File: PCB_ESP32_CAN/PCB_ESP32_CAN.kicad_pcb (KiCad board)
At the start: 2 copper layers, 52.1 x 57.2 mm, 53 parts, among them J1 USB_C_Receptacle_USB2.0, J2 CAN, J3 CAN, J4 CAN, J5 CAN, Q1 Q_NPN_BCE, Q2 Q_NPN_BCE, U1 ESP32-WROOM-32, U2 CP2102N-A01-GQFN24, U3 SN65HVD232, U4 NCP1117-3.3_SOT223

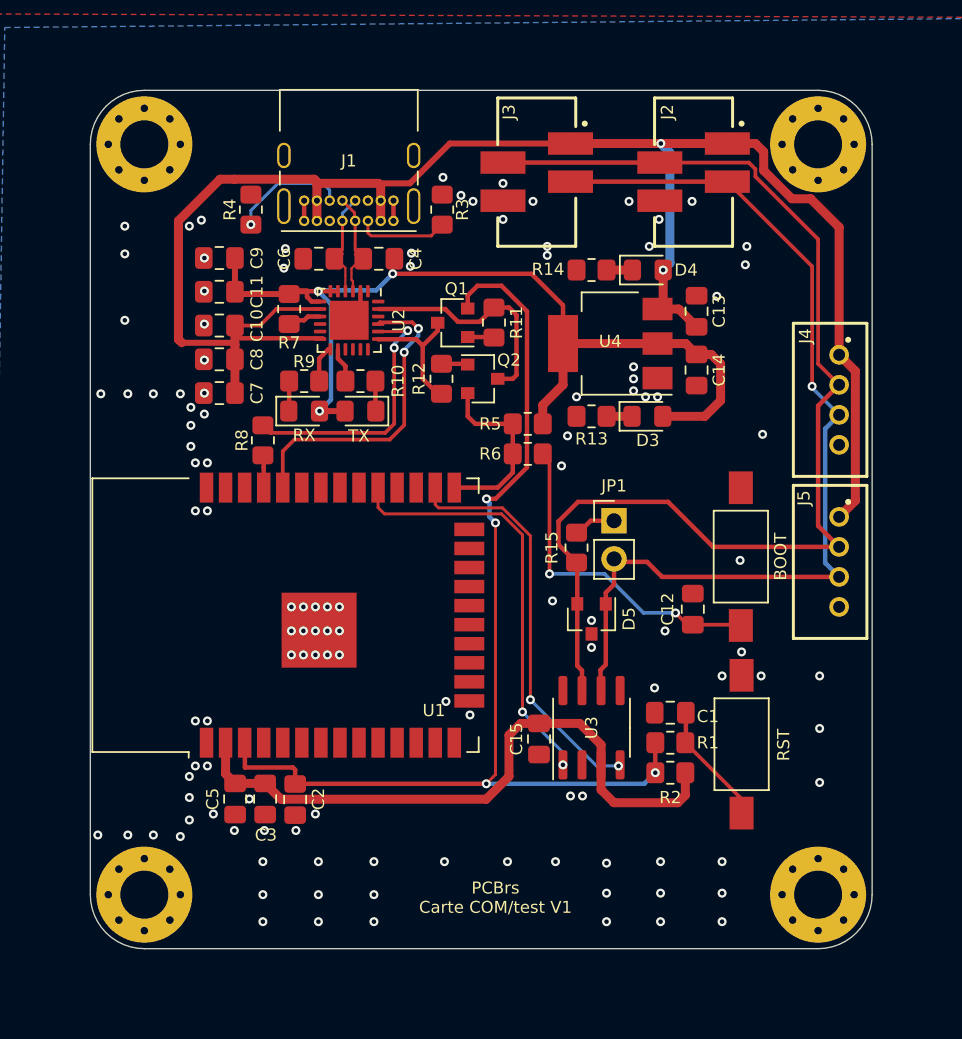
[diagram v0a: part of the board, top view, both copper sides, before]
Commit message: pcb lidar/ax12/batt ready to fab
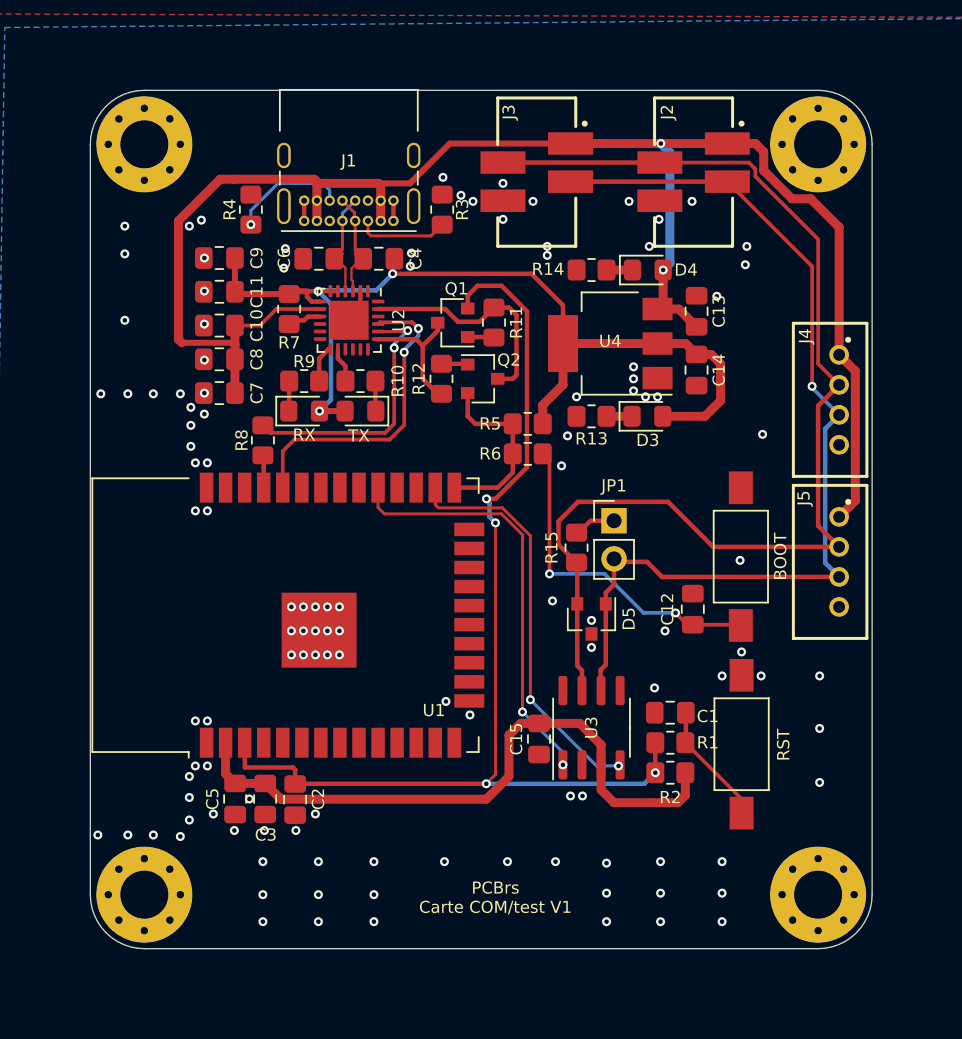
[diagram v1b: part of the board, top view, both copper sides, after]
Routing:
- net Net-(U2-Pad12): track 5.52 -> 0.00 mm
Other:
- net class Default removed

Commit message: V2.0 ESP32 pcb
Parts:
- removed J4, J5: CAN, AREA_lib_Connector:Wuerth_2mm_4pin_62000411622
- removed R1, R6: 560, Resistor_SMD:R_0805_2012Metric_Pad1.20x1.40mm_HandSolder
- removed R5: 10K, Resistor_SMD:R_0805_2012Metric_Pad1.20x1.40mm_HandSolder
- added C16: 10u, Capacitor_SMD:C_0805_2012Metric_Pad1.18x1.45mm_HandSolder, F.Cu at (156.1, 123.2)
- added CANH: CANH, TestPoint:TestPoint_THTPad_D1.0mm_Drill0.5mm, F.Cu at (158.3, 101.6)
- added CANL: CANL, TestPoint:TestPoint_THTPad_D1.0mm_Drill0.5mm, F.Cu at (158.3, 103.5)
- added DTR: DTR, TestPoint:TestPoint_Pad_D1.0mm, F.Cu at (136.4, 86.2)
- added R16: 47k5, Resistor_SMD:R_0805_2012Metric_Pad1.20x1.40mm_HandSolder, F.Cu at (123.7, 90.7)
- added R17: 10k, Resistor_SMD:R_0805_2012Metric_Pad1.20x1.40mm_HandSolder, F.Cu at (123.7, 88.7)
- added RTS: RTS, TestPoint:TestPoint_Pad_D1.0mm, F.Cu at (135.5, 90.2)
- added RX: RX, TestPoint:TestPoint_Pad_D1.0mm, F.Cu at (131.2, 118.9)
- added TX: TX, TestPoint:TestPoint_Pad_D1.0mm, F.Cu at (131.2, 115.7)
- C1, C12, C2: value 1n -> 100n
- R10: value 260 -> 270
- R7: value 10K -> 22k1
- moved C5 93.9 mm to (156.1, 121.2), turned to 0 degrees
- moved C3 91.8 mm to (156.1, 119.2), turned to 0 degrees
- moved C2 89.8 mm to (156.1, 117.2), turned to 180 degrees
- moved J3 80.9 mm to (160.4, 96.4), turned to 180 degrees
- moved U1 75.8 mm to (143.8, 114.5), turned to 180 degrees
- moved R8 68.7 mm to (129.0, 115.7)
- moved J2 68.4 mm to (160.4, 86.0), turned to 180 degrees
- moved R15 65.8 mm to (150.8, 99.2), turned to 0 degrees
- moved 120 65.1 mm to (152.5, 101.7), turned to -90 degrees
- moved C10 63.2 mm to (123.7, 94.7)
- moved C8 63.2 mm to (123.7, 96.8)
- moved C7 63.1 mm to (123.7, 98.8)
- moved C9 62.6 mm to (123.7, 84.7)
- moved C11 62.6 mm to (123.7, 86.7)
- moved R10 61.8 mm to (132.2, 93.5)
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- renumbered JP1 to 120, D3 to 3V3, D4 to 5V, RST to RESET
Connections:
- BOOT pad 1: Net-(C12-Pad1) -> /IO0
- C1 pad 1: Net-(C1-Pad1) -> /EN
- C12 pad 1: Net-(C12-Pad1) -> /IO0
- J1 pad A8: Net-(J1-PadA8) -> unconnected-(J1-PadA8)
- J1 pad B8: Net-(J1-PadB8) -> unconnected-(J1-PadB8)
- R10 pad 1: Net-(D2-Pad1) -> Net-(D2-Pad2)
- R7 pad 1: +3V3 -> +5V
- R7 pad 2: Net-(R7-Pad2) -> Net-(R16-Pad1)
- R9 pad 1: Net-(D1-Pad1) -> Net-(D1-Pad2)
- RESET pad 1: Net-(C1-Pad1) -> GND
- RESET pad 2: GND -> /EN
- RX pad 1: Net-(D1-Pad1) -> GND
- RX pad 2: +3V3 -> Net-(D1-Pad2)
- TX pad 1: Net-(D2-Pad1) -> GND
- TX pad 2: +3V3 -> Net-(D2-Pad2)
- U1 pad 10: Net-(U1-Pad10) -> unconnected-(U1-Pad10)
- U1 pad 11: Net-(U1-Pad11) -> unconnected-(U1-Pad11)
- U1 pad 12: Net-(U1-Pad12) -> unconnected-(U1-Pad12)
- U1 pad 13: Net-(U1-Pad13) -> unconnected-(U1-Pad13)
- U1 pad 14: Net-(U1-Pad14) -> unconnected-(U1-Pad14)
- U1 pad 16: Net-(U1-Pad16) -> unconnected-(U1-Pad16)
- U1 pad 17: Net-(U1-Pad17) -> unconnected-(U1-Pad17)
- U1 pad 18: Net-(U1-Pad18) -> unconnected-(U1-Pad18)
- U1 pad 19: Net-(U1-Pad19) -> unconnected-(U1-Pad19)
- U1 pad 20: Net-(U1-Pad20) -> unconnected-(U1-Pad20)
- U1 pad 21: Net-(U1-Pad21) -> unconnected-(U1-Pad21)
- U1 pad 22: Net-(U1-Pad22) -> unconnected-(U1-Pad22)
- U1 pad 23: Net-(U1-Pad23) -> unconnected-(U1-Pad23)
- U1 pad 24: Net-(U1-Pad24) -> unconnected-(U1-Pad24)
- U1 pad 27: Net-(U1-Pad27) -> unconnected-(U1-Pad27)
- U1 pad 28: Net-(U1-Pad28) -> unconnected-(U1-Pad28)
- U1 pad 30: Net-(U1-Pad30) -> unconnected-(U1-Pad30)
- U1 pad 31: Net-(U1-Pad31) -> unconnected-(U1-Pad31)
- U1 pad 32: Net-(U1-Pad32) -> unconnected-(U1-Pad32)
- U1 pad 33: Net-(U1-Pad33) -> unconnected-(U1-Pad33)
- U1 pad 36: Net-(U1-Pad36) -> unconnected-(U1-Pad36)
- U1 pad 37: Net-(U1-Pad37) -> unconnected-(U1-Pad37)
- U1 pad 4: Net-(U1-Pad4) -> unconnected-(U1-Pad4)
- U1 pad 5: Net-(U1-Pad5) -> unconnected-(U1-Pad5)
- U1 pad 6: Net-(U1-Pad6) -> unconnected-(U1-Pad6)
- U1 pad 7: Net-(U1-Pad7) -> unconnected-(U1-Pad7)
- U1 pad 8: Net-(U1-Pad8) -> unconnected-(U1-Pad8)
- U1 pad 9: Net-(U1-Pad9) -> unconnected-(U1-Pad9)
- U2 pad 1: Net-(U2-Pad1) -> unconnected-(U2-Pad1)
- U2 pad 10: Net-(U2-Pad10) -> unconnected-(U2-Pad10)
- U2 pad 11: Net-(U2-Pad11) -> unconnected-(U2-Pad11)
- U2 pad 12: Net-(U2-Pad12) -> unconnected-(U2-Pad12)
- U2 pad 15: Net-(U2-Pad15) -> unconnected-(U2-Pad15)
- U2 pad 16: Net-(U2-Pad16) -> unconnected-(U2-Pad16)
- U2 pad 17: Net-(U2-Pad17) -> unconnected-(U2-Pad17)
- U2 pad 18: Net-(U2-Pad18) -> unconnected-(U2-Pad18)
- U2 pad 22: Net-(U2-Pad22) -> unconnected-(U2-Pad22)
- U2 pad 24: Net-(U2-Pad24) -> unconnected-(U2-Pad24)
- U2 pad 5: +3V3 -> unconnected-(U2-Pad5)
- U2 pad 8: +5V -> Net-(R16-Pad1)
- U2 pad 9: Net-(R7-Pad2) -> Net-(U2-Pad9)
- U3 pad 5: Net-(U3-Pad5) -> unconnected-(U3-Pad5)
- U3 pad 8: Net-(U3-Pad8) -> unconnected-(U3-Pad8)
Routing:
- net +5V: track 112.2 -> 9.81 mm, vias 2 -> 11
- net +3V3: track 108.1 -> 35.7 mm, vias 3 -> 14
- net /CANH: track 78.0 -> 32.6 mm
- net /CANL: track 65.3 -> 37.5 mm, vias 1 -> 0
- net /IO0: track 12.3 -> 37.5 mm, vias 0 -> 3
- net Net-(C12-Pad1): track 22.4 -> 0.00 mm, vias 2 -> 0
- net /RXCAN: track 27.2 -> 9.71 mm, vias 2 -> 0
- net /TX: track 21.0 -> 36.1 mm
- net Net-(R8-Pad2): track 17.8 -> 29.1 mm
- net /EN: track 71.6 -> 82.2 mm
- net Net-(C1-Pad1): track 8.26 -> 0.00 mm
- net /TXCAN: track 28.1 -> 20.5 mm, vias 2 -> 0
- net Net-(R16-Pad1): track 0.00 -> 6.97 mm
- net Net-(U2-Pad9): track 0.00 -> 6.20 mm, vias 0 -> 2
- net /RX: track 2.31 -> 7.25 mm
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- added copper zone on In1.Cu, net +3V3
- added copper zone on In1.Cu, net +5V
- added copper zone on In2.Cu, net GND
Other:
- copper layers 2 -> 4
- board text added: "."
- board text added: "PCBrs Carte COM V2 IP : 192.168.4.1"
- board text removed: "PCBrs Carte COM/test V1"

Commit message: update
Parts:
- C1, C10, C11, C12, C13, C14, C15, C16, C2, C3, C4, C5, C6, C7, C8, C9: footprint Capacitor_SMD:C_0805_2012Metric_Pad1.18x1.45mm_HandSolder -> Capacitor_SMD:C_0805_2012Metric
- D1: renamed from RX; footprint LED_SMD:LED_0805_2012Metric_Pad1.15x1.40mm_HandSolder -> LED_SMD:LED_0805_2012Metric
- D2: renamed from TX; footprint LED_SMD:LED_0805_2012Metric_Pad1.15x1.40mm_HandSolder -> LED_SMD:LED_0805_2012Metric
- D3: renamed from 3V3; footprint LED_SMD:LED_0805_2012Metric_Pad1.15x1.40mm_HandSolder -> LED_SMD:LED_0805_2012Metric
- D4: renamed from 5V; footprint LED_SMD:LED_0805_2012Metric_Pad1.15x1.40mm_HandSolder -> LED_SMD:LED_0805_2012Metric
- Q1, Q2: value Q_NPN_BCE -> MMBT2222ALT1G
- R10, R11, R12, R13, R14, R15, R16, R17, R2, R3, R4, R7, R8, R9: footprint Resistor_SMD:R_0805_2012Metric_Pad1.20x1.40mm_HandSolder -> Resistor_SMD:R_0805_2012Metric
- TP5: renamed from CANH; footprint TestPoint:TestPoint_THTPad_D1.0mm_Drill0.5mm -> TestPoint:TestPoint_Pad_D1.0mm
- TP6: renamed from CANL; footprint TestPoint:TestPoint_THTPad_D1.0mm_Drill0.5mm -> TestPoint:TestPoint_Pad_D1.0mm
- moved R2 10.2 mm to (128.8, 120.1), turned to -90 degrees
- moved SW2 7.53 mm to (123.7, 106.9)
- moved SW1 7.46 mm to (123.7, 118.9)
- moved C1 6.33 mm to (126.7, 120.1), turned to 90 degrees
- moved C12 6.01 mm to (126.7, 103.4), turned to -90 degrees
- moved H1 3.24 mm to (120.1, 77.1)
- moved H2 3.24 mm to (120.1, 127.1)
- moved TP6 1.39 mm to (159.4, 102.7)
- moved D3 1.15 mm to (149.8, 96.2)
- moved C13 1.15 mm to (153.1, 89.2)
- moved D4 1.15 mm to (149.8, 86.4)
- moved R13 1.15 mm to (146.1, 96.2)
- moved R14 1.15 mm to (146.1, 86.4)
- moved U4 1.15 mm to (147.3, 91.3)
- moved C14 0.88 mm to (153.1, 92.7)
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- renumbered 120 to JP1, RESET to SW1, BOOT to SW2, RTS to TP1, DTR to TP2, RX to TP3, TX to TP4
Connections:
- D1 pad 1: GND -> +3V3
- D2 pad 1: GND -> +3V3
- Q1 pad 2: /EN -> /RTS
- Q1 pad 3: /RTS -> /EN
- Q2 pad 2: /IO0 -> /DTR
- Q2 pad 3: /DTR -> /IO0
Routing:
- net +5V: track 9.81 -> 18.6 mm
- net /EN: track 82.2 -> 77.1 mm
- net /IO0: track 37.5 -> 33.2 mm
- net /DTR: track 16.3 -> 19.9 mm
- net Net-(R17-Pad2): track 6.20 -> 9.44 mm
- net +3V3: track 35.7 -> 38.9 mm, vias 14 -> 15
- net /RTS: track 9.76 -> 11.4 mm
- net Net-(J1-PadA5): track 5.99 -> 7.11 mm
- net Net-(R10-Pad2): track 3.36 -> 3.92 mm
- net GND: vias 44 -> 82
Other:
- board size 52.1 x 57.2 mm -> 48.9 x 57.2 mm
